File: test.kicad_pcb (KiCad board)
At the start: 2 copper layers, 100 x 100 mm, 165 parts, among them Q1 T2N7002AK, Q2 T2N7002AK, U1 ESP32-S3-WROOM-1, U2 LD1117S33TR_SOT223, U3 SN75176AD, U4 LM321, U5 LM2576HVS-5, U6 MAX31855KASA

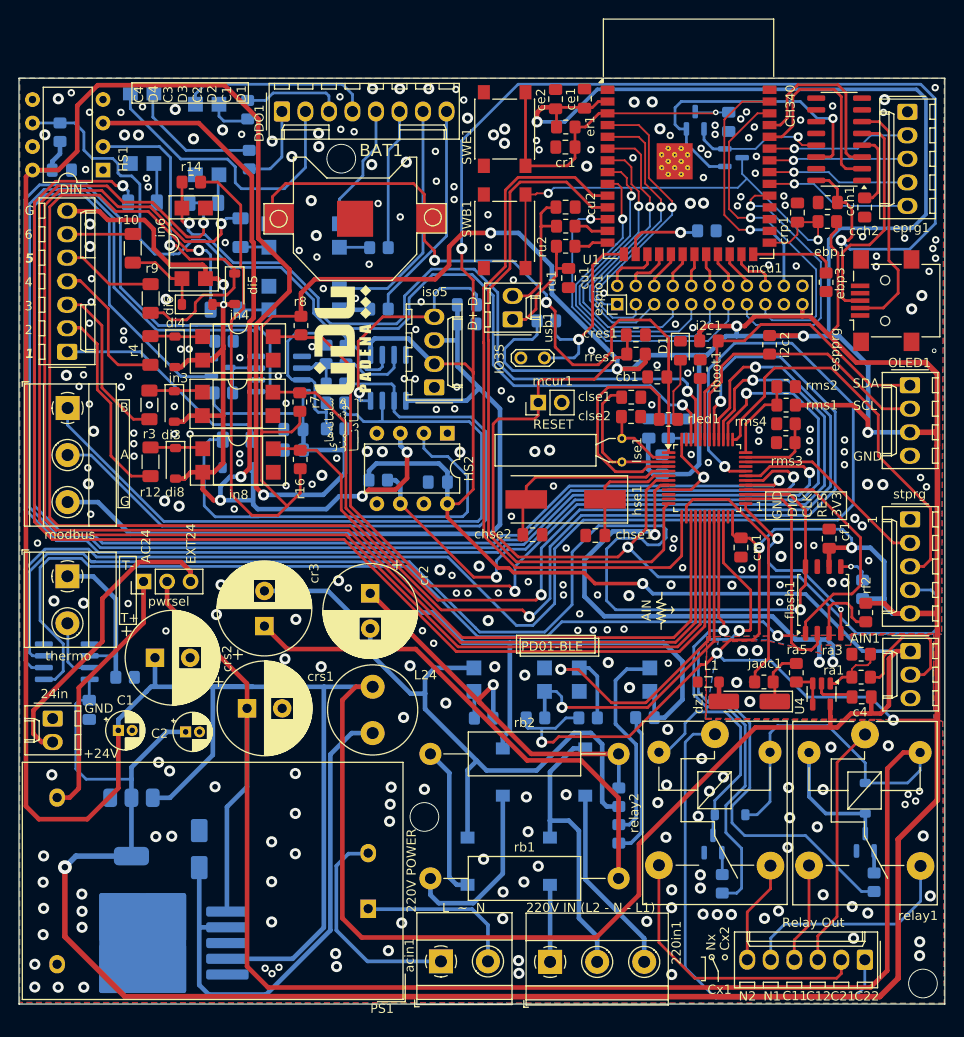
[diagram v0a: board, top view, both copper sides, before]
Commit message: changed ESP32 fottprint
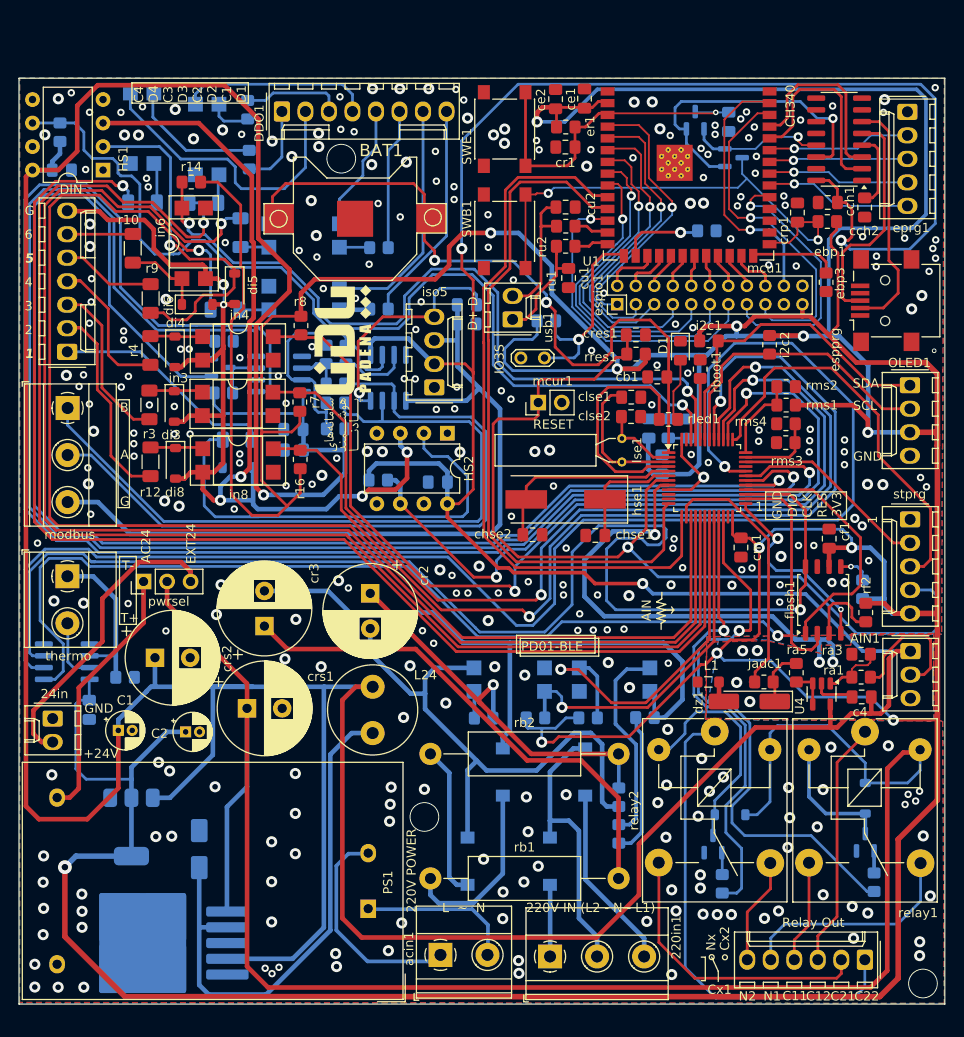
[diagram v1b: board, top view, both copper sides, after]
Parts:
- moved acin1 0.71 mm to (45.6, 94.5)
- moved 220in1 0.58 mm to (57.4, 94.7)
- moved relay1 0.30 mm to (91.4, 70.4)
- moved relay2 0.28 mm to (75.2, 70.4)
- moved U1 0.17 mm to (72.4, 6.47)
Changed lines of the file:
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@@
 			(drillshape 0)
 			(scaleselection 1)
-			(outputdirectory "/home/iman/kicad-test/test/gerber/")
+			(outputdirectory "/home/iman/kicad-test/test/gerber/v2/")
 		)
 	)
@@
 	(footprint "Relay_THT:Relay_SPDT_SANYOU_SRD_Series_Form_C"
 		(layer "F.Cu")
-		(at 75.21 70.64 -90)
+		(at 75.19 70.36 -90)
 		(descr "relay Sanyou SRD series Form C http://www.sanyourelay.ca/public/products/pdf/SRD.pdf")
 		(tags "relay Sanyu SRD form C")
@@
 		(tags "ACDC-Converter 5W THT Hi-Link board mount module")
 		(property "Reference" "PS1"
-			(at -1.5 -10.79 180)
+			(at -2.1425 2.8375 -90)
 			(layer "F.SilkS")
 			(effects
@@
 	(footprint "Relay_THT:Relay_SPDT_SANYOU_SRD_Series_Form_C"
 		(layer "F.Cu")
-		(at 91.42 70.67 -90)
+		(at 91.42 70.37 -90)
 		(descr "relay Sanyou SRD series Form C http://www.sanyourelay.ca/public/products/pdf/SRD.pdf")
 		(tags "relay Sanyu SRD form C")
@@
 	(footprint "TerminalBlock_Phoenix:TerminalBlock_Phoenix_MKDS-1,5-3-5.08_1x03_P5.08mm_Horizontal"
 		(layer "F.Cu")
-		(at 57.41 95.23)
+		(at 57.4 94.65)
 		(descr "Terminal Block Phoenix MKDS-1,5-3-5.08, 3 pins, pitch 5.08mm, size 15.2x9.8mm^2, drill diamater 1.3mm, pad diameter 2.6mm, see http://www.farnell.com/datasheets/100425.pdf, script-generated using https://github.com/pointhi/kicad-footprint-generator/scripts/TerminalBlock_Phoenix")
 		(tags "THT Terminal Block Phoenix MKDS-1,5-3-5.08 pitch 5.08mm size 15.2x9.8mm^2 drill 1.3mm pad 2.6mm")
@@
 	(footprint "TerminalBlock_Phoenix:TerminalBlock_Phoenix_MKDS-1,5-2-5.08_1x02_P5.08mm_Horizontal"
 		(layer "F.Cu")
-		(at 45.615 95.18)
+		(at 45.565 94.475)
 		(descr "Terminal Block Phoenix MKDS-1,5-2-5.08, 2 pins, pitch 5.08mm, size 10.2x9.8mm^2, drill diamater 1.3mm, pad diameter 2.6mm, see http://www.farnell.com/datasheets/100425.pdf, script-generated using https://github.com/pointhi/kicad-footprint-generator/scripts/TerminalBlock_Phoenix")
 		(tags "THT Terminal Block Phoenix MKDS-1,5-2-5.08 pitch 5.08mm size 10.2x9.8mm^2 drill 1.3mm pad 2.6mm")
@@
 	(footprint "RF_Module:ESP32-S3-WROOM-1"
 		(layer "F.Cu")
-		(at 72.36 6.3)
+		(at 72.36 6.47)
 		(descr "2.4 GHz Wi-Fi and Bluetooth module  https://www.espressif.com/sites/default/files/documentation/esp32-s3-wroom-1_wroom-1u_datasheet_en.pdf")
 		(tags "2.4 GHz Wi-Fi and Bluetooth module")
@@
 		(attr smd)
 		(fp_line
-			(start -9.2 -12.9)
-			(end -9.2 -6.7)
-			(stroke
-				(width 0.12)
-				(type solid)
-			)
-			(layer "F.SilkS")
-		)
-		(fp_line
-			(start -9.2 -12.9)
-			(end 9.2 -12.9)
-			(stroke
-				(width 0.12)
-				(type solid)
-			)
-			(layer "F.SilkS")
-		)
-		(fp_line
 			(start -9.2 11.95)
 			(end -9.2 12.95)
@@
 		)
 		(fp_line
-			(start 9.2 -12.9)
-			(end 9.2 -6.7)
-			(stroke
-				(width 0.12)
-				(type solid)
-			)
-			(layer "F.SilkS")
-		)
-		(fp_line
 			(start 9.2 12.95)
 			(end 7.7 12.95)
@@
 			(layer "F.SilkS")
 		)
-		(fp_poly
-			(pts
-				(xy -9.2 -6.025) (xy -9.7 -6.025) (xy -9.2 -6.525) (xy -9.2 -6.025)
-			)
-			(stroke
-				(width 0.12)
-				(type solid)
-			)
-			(fill solid)
-			(layer "F.SilkS")
-		)
-		(fp_line
-			(start -24 -27.75)
-			(end -24 -6.75)
-			(stroke
-				(width 0.05)
-				(type solid)
-			)
-			(layer "F.CrtYd")
-		)
 		(fp_line
-			(start -24 -6.75)
-			(end -9.75 -6.75)
+			(start -9.76 -6.17)
+			(end 9.74 -6.17)
 			(stroke
 				(width 0.05)
-				(type solid)
+				(type default)
 			)
 			(layer "F.CrtYd")
+			(net 9)
 		)
 		(fp_line
 			(start -9.75 13.45)
-			(end -9.75 -6.75)
+			(end -9.76 -6.17)
 			(stroke
 				(width 0.05)
@@
 		)
 		(fp_line
-			(start 9.75 -6.75)
+			(start 9.74 -6.17)
 			(end 9.75 13.45)
 			(stroke
@@
 		)
 		(fp_line
-			(start 9.75 -6.75)
-			(end 24 -6.75)
-			(stroke
-				(width 0.05)
-				(type solid)
-			)
-			(layer "F.CrtYd")
-		)
-		(fp_line
-			(start 24 -27.75)
-			(end -24 -27.75)
-			(stroke
-				(width 0.05)
-				(type solid)
-			)
-			(layer "F.CrtYd")
-		)
-		(fp_line
-			(start 24 -6.75)
-			(end 24 -27.75)
-			(stroke
-				(width 0.05)
-				(type solid)
-			)
-			(layer "F.CrtYd")
-		)
-		(fp_line
-			(start -9 -12.75)
-			(end 9 -12.75)
-			(stroke
-				(width 0.1)
-				(type solid)
-			)
-			(layer "F.Fab")
-		)
-		(fp_line
-			(start -9 -6.75)
-			(end 9 -6.75)
-			(stroke
-				(width 0.1)
-				(type solid)
-			)
-			(layer "F.Fab")
-		)
-		(fp_line
-			(start -9 12.75)
-			(end -9 -12.75)
+			(start -9.07 -6.16)
+			(end 8.93 -6.16)
 			(stroke
 				(width 0.1)
@@
 			(layer "F.Fab")
 		)
-		(fp_line
-			(start 9 12.75)
-			(end 9 -12.75)
-			(stroke
-				(width 0.1)
-				(type solid)
-			)
-			(layer "F.Fab")
-		)
-		(fp_text user "Antenna"
-			(at -0.05 -9.44 0)
-			(layer "Cmts.User")
-			(effects
-				(font
-					(size 1 1)
-					(thickness 0.15)
-				)
-			)
-		)
-		(fp_text user "KEEP-OUT ZONE"
-			(at 0 -18.92 0)
-			(layer "Cmts.User")
-			(effects
-				(font
-					(size 2 2)
-					(thickness 0.15)
-				)
-			)
-		)
 		(fp_text user "${REFERENCE}"
 			(at 0 -0.6 0)
@@
 			(pintype "passive")
 		)
-		(zone
-			(net 0)
-			(net_name "")
-			(layers "F.Cu" "In1.Cu" "B.Cu")
-			(hatch full 0.508)
-			(connect_pads
-				(clearance 0)
-			)
-			(min_thickness 0.254)
-			(filled_areas_thickness no)
-			(keepout
-				(tracks not_allowed)
-				(vias not_allowed)
-				(pads not_allowed)
-				(copperpour not_allowed)
-				(footprints not_allowed)
-			)
-			(fill
-				(thermal_gap 0.508)
-				(thermal_bridge_width 0.508)
-			)
-			(polygon
-				(pts
-					(xy 48.36 -0.45) (xy 96.36 -0.45) (xy 96.36 -21.45) (xy 48.36 -21.45)
-				)
-			)
-		)
 		(model "${KICAD8_3DMODEL_DIR}/RF_Module.3dshapes/ESP32-S3-WROOM-1.wrl"
 			(offset
@@
 	)
 	(via
-		(at 70.53 89.38)
+		(at 71.01 89.73)
 		(size 1.2)
 		(drill 0.6)
@@
 	)
 	(segment
-		(start 77.05 78.39)
-		(end 77.05 80.22)
+		(start 74.477106 67.19)
+		(end 76.724214 67.19)
 		(width 0.3)
 		(layer "B.Cu")
@@
 	)
 	(segment
-		(start 74.477106 67.19)
-		(end 76.724214 67.19)
+		(start 73.43 66.142894)
+		(end 74.477106 67.19)
 		(width 0.3)
 		(layer "B.Cu")
@@
 	)
 	(segment
-		(start 73.43 66.142894)
-		(end 74.477106 67.19)
+		(start 78.98 69.445786)
+		(end 78.98 76.445199)
 		(width 0.3)
 		(layer "B.Cu")
@@
 	)
 	(segment
-		(start 78.42 81.59)
-		(end 85 81.59)
+		(start 85.6 81.59)
+		(end 91.640356 87.630356)
 		(width 0.3)
 		(layer "B.Cu")
@@
 	)
 	(segment
-		(start 78.98 69.445786)
-		(end 78.98 76.445199)
+		(start 76.88 60.4)
+		(end 74.58 60.4)
 		(width 0.3)
 		(layer "B.Cu")
@@
 	)
 	(segment
-		(start 91.040356 87.630356)
+		(start 91.640356 87.630356)
 		(end 92.4 87.630356)
 		(width 0.3)
@@
 	)
 	(segment
-		(start 77.05 80.22)
-		(end 78.42 81.59)
+		(start 78.42 81.59)
+		(end 85.6 81.59)
 		(width 0.3)
 		(layer "B.Cu")
@@
 	)
 	(segment
-		(start 76.88 60.4)
-		(end 74.58 60.4)
+		(start 78.98 76.46)
+		(end 77.05 78.39)
 		(width 0.3)
 		(layer "B.Cu")
@@
 	)
 	(segment
-		(start 78.98 76.46)
-		(end 77.05 78.39)
+		(start 77.05 80.22)
+		(end 78.42 81.59)
 		(width 0.3)
 		(layer "B.Cu")
@@
 	)
 	(segment
-		(start 85 81.59)
-		(end 91.040356 87.630356)
+		(start 77.05 78.39)
+		(end 77.05 80.22)
 		(width 0.3)
 		(layer "B.Cu")
